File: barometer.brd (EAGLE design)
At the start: 58.4 x 40.4 mm, 91 parts, among them IC1 MIC5225-3.3v, IC2 TPS5410, IC3 ZPA2326-0311A-R, U1 MCP4725, U2 LTC2850, U3 PCA9306, U4 MAX3221, U5 XC6215XC6215B182NR, U6 Tiny85-20-SMT, X2 1751264, X3 1751248

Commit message: Migrate to customised/forked libraries
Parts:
- SJ1, SJ10, SJ11, SJ12, SJ2, SJ3, SJ4, SJ5, SJ6, SJ7, SJ8, SJ9: device SparkFun-Retired:SJ_2S-TRACE -> SparkFun-Retired-0:SJ_2S-TRACE
- U3: device SparkFun-IC-Comms:PSOP-8 -> v-shifter-sparkfun:PSOP-8
- U6: device SparkFun-Retired:SO08-EIAJ_MCU -> SparkFun-Retired-0:SO08-EIAJ_MCU
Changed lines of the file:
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@@
 <attribute name="TP_SIGNAL_NAME" value="" x="31.6625" y="17.6425" size="1" layer="38" rot="MR0"/>
 </element>
-<element name="SJ1" library="SparkFun-Retired" package="SJ_2S-TRACE" value="SOLDERJUMPERTRACE" x="55.8875" y="9.3675" smashed="yes" rot="MR90">
+<element name="SJ1" library="SparkFun-Retired-0" package="SJ_2S-TRACE" value="SOLDERJUMPERTRACE" x="55.8875" y="9.3675" smashed="yes" rot="MR90">
 <attribute name="NAME" x="53.8875" y="8.455" size="0.8128" layer="26" font="vector" ratio="18" rot="MR90"/>
 </element>
-<element name="SJ2" library="SparkFun-Retired" package="SJ_2S-TRACE" value="SOLDERJUMPERTRACE" x="52.3875" y="9.3875" smashed="yes" rot="MR90">
+<element name="SJ2" library="SparkFun-Retired-0" package="SJ_2S-TRACE" value="SOLDERJUMPERTRACE" x="52.3875" y="9.3875" smashed="yes" rot="MR90">
 <attribute name="NAME" x="51.8555" y="5.685" size="0.8128" layer="26" font="vector" ratio="18" rot="MR90"/>
 </element>
-<element name="SJ3" library="SparkFun-Retired" package="SJ_2S-TRACE" value="SOLDERJUMPERTRACE" x="47.3075" y="7.6175" smashed="yes" rot="MR90">
+<element name="SJ3" library="SparkFun-Retired-0" package="SJ_2S-TRACE" value="SOLDERJUMPERTRACE" x="47.3075" y="7.6175" smashed="yes" rot="MR90">
 <attribute name="NAME" x="45.1765" y="7.205" size="0.8128" layer="26" font="vector" ratio="18" rot="MR90"/>
 </element>
-<element name="SJ4" library="SparkFun-Retired" package="SJ_2S-TRACE" value="SOLDERJUMPERTRACE" x="49.8075" y="7.6175" smashed="yes" rot="MR90">
+<element name="SJ4" library="SparkFun-Retired-0" package="SJ_2S-TRACE" value="SOLDERJUMPERTRACE" x="49.8075" y="7.6175" smashed="yes" rot="MR90">
 <attribute name="NAME" x="47.4225" y="6.09" size="0.8128" layer="26" font="vector" ratio="18" rot="MR180"/>
 </element>
@@
 <attribute name="TP_SIGNAL_NAME" value="" x="29.1225" y="21.4525" size="1" layer="38" rot="MR0"/>
 </element>
-<element name="U6" library="SparkFun-Retired" package="SO08-EIAJ_MCU" value="Tiny85-20-SMT" x="18.0975" y="29.8425" smashed="yes" rot="MR180">
+<element name="U6" library="SparkFun-Retired-0" package="SO08-EIAJ_MCU" value="Tiny85-20-SMT" x="18.0975" y="29.8425" smashed="yes" rot="MR180">
 <attribute name="NAME" x="21.59" y="27.3025" size="0.8128" layer="26" font="vector" ratio="18" rot="MR270"/>
 <attribute name="PROD_ID" value="IC-09092" x="18.0975" y="29.8425" size="1.778" layer="28" rot="MR180" display="off"/>
 </element>
-<element name="SJ5" library="SparkFun-Retired" package="SJ_2S-TRACE" value="SOLDERJUMPERTRACE" x="24.13" y="28.89" smashed="yes">
+<element name="SJ5" library="SparkFun-Retired-0" package="SJ_2S-TRACE" value="SOLDERJUMPERTRACE" x="24.13" y="28.89" smashed="yes">
 <attribute name="NAME" x="22.36" y="26.91" size="0.8128" layer="25" font="vector" ratio="18"/>
 </element>
-<element name="SJ6" library="SparkFun-Retired" package="SJ_2S-TRACE" value="SOLDERJUMPERTRACE" x="19.05" y="30.4775" smashed="yes" rot="MR90">
+<element name="SJ6" library="SparkFun-Retired-0" package="SJ_2S-TRACE" value="SOLDERJUMPERTRACE" x="19.05" y="30.4775" smashed="yes" rot="MR90">
 <attribute name="NAME" x="20.6375" y="28.5725" size="0.8128" layer="26" font="vector" ratio="18" rot="MR90"/>
 </element>
-<element name="SJ7" library="SparkFun-Retired" package="SJ_2S-TRACE" value="SOLDERJUMPERTRACE" x="24.13" y="28.89" smashed="yes" rot="MR180">
+<element name="SJ7" library="SparkFun-Retired-0" package="SJ_2S-TRACE" value="SOLDERJUMPERTRACE" x="24.13" y="28.89" smashed="yes" rot="MR180">
 <attribute name="NAME" x="25.4" y="27.62" size="0.8128" layer="26" font="vector" ratio="18" rot="MR90"/>
 </element>
-<element name="SJ8" library="SparkFun-Retired" package="SJ_2S-TRACE" value="SOLDERJUMPERTRACE" x="24.13" y="30.795" smashed="yes" rot="MR180">
+<element name="SJ8" library="SparkFun-Retired-0" package="SJ_2S-TRACE" value="SOLDERJUMPERTRACE" x="24.13" y="30.795" smashed="yes" rot="MR180">
 <attribute name="NAME" x="25.4" y="29.8425" size="0.8128" layer="26" font="vector" ratio="18" rot="MR90"/>
 </element>
-<element name="SJ9" library="SparkFun-Retired" package="SJ_2S-TRACE" value="SOLDERJUMPERTRACE" x="17.145" y="30.4775" smashed="yes" rot="MR90">
+<element name="SJ9" library="SparkFun-Retired-0" package="SJ_2S-TRACE" value="SOLDERJUMPERTRACE" x="17.145" y="30.4775" smashed="yes" rot="MR90">
 <attribute name="NAME" x="15.28" y="31.005" size="0.8128" layer="26" font="vector" ratio="18" rot="MR0"/>
 </element>
@@
 <attribute name="OC_NEWARK" value="10R0934" x="44.02" y="3.4" size="1.778" layer="27" rot="R180" display="off"/>
 </element>
-<element name="U3" library="SparkFun-IC-Comms" package="PSOP-8" value="PCA9306" x="14.605" y="19.0475" smashed="yes" rot="R180">
+<element name="U3" library="v-shifter-sparkfun" package="PSOP-8" value="PCA9306" x="14.605" y="19.0475" smashed="yes" rot="R180">
 <attribute name="NAME" x="13.081" y="19.5475" size="0.6096" layer="21" font="vector" ratio="18" rot="SR270" align="center"/>
 <attribute name="PROD_ID" value="IC-10023" x="14.605" y="19.0475" size="1.778" layer="27" rot="R180" display="off"/>
 </element>
-<element name="SJ10" library="SparkFun-Retired" package="SJ_2S-TRACE" value="SOLDERJUMPERTRACE" x="24.75" y="35.25" smashed="yes" rot="MR180">
+<element name="SJ10" library="SparkFun-Retired-0" package="SJ_2S-TRACE" value="SOLDERJUMPERTRACE" x="24.75" y="35.25" smashed="yes" rot="MR180">
 <attribute name="NAME" x="23.7975" y="37.23" size="0.8128" layer="26" font="vector" ratio="18" rot="MR180"/>
 </element>
-<element name="SJ11" library="SparkFun-Retired" package="SJ_2S-TRACE" value="SOLDERJUMPERTRACE" x="24.75" y="35.25" smashed="yes">
+<element name="SJ11" library="SparkFun-Retired-0" package="SJ_2S-TRACE" value="SOLDERJUMPERTRACE" x="24.75" y="35.25" smashed="yes">
 <attribute name="NAME" x="23.7975" y="36.52" size="0.8128" layer="25" font="vector" ratio="18"/>
 </element>
@@
 <attribute name="TP_SIGNAL_NAME" value="" x="40.51" y="34.2675" size="1" layer="38" rot="MR0"/>
 </element>
-<element name="SJ12" library="SparkFun-Retired" package="SJ_2S-TRACE" value="SOLDERJUMPERTRACE" x="24.13" y="30.795" smashed="yes">
+<element name="SJ12" library="SparkFun-Retired-0" package="SJ_2S-TRACE" value="SOLDERJUMPERTRACE" x="24.13" y="30.795" smashed="yes">
 <attribute name="NAME" x="22.113325" y="31.9944625" size="0.8128" layer="25" font="vector" ratio="18" rot="R90" align="bottom-right"/>
 </element>

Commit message: Update all libraries
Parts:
- D2: value B340A -> 3A/40V/500mV
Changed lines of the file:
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@@
 </autorouter>
 <elements>
-<element name="D1" library="adafruit" package="SOD-123FL" value="SCHOTTKY" x="30.0075" y="13.9675" smashed="yes" rot="MR0">
+<element name="D1" library="adafruit" library_urn="urn:adsk.eagle:library:420" package="SOD-123FL" value="SCHOTTKY" x="30.0075" y="13.9675" smashed="yes" rot="MR0">
 <attribute name="NAME" x="33.6475" y="13.6975" size="0.8128" layer="26" font="vector" ratio="18" rot="MR0"/>
 </element>
-<element name="IC1" library="adafruit" package="SOT23-5L" value="MIC5225-3.3v" x="36.195" y="13.9675" smashed="yes" rot="MR90">
+<element name="IC1" library="adafruit" library_urn="urn:adsk.eagle:library:420" package="SOT23-5L" value="MIC5225-3.3v" x="36.195" y="13.9675" smashed="yes" rot="MR90">
 <attribute name="NAME" x="38.4175" y="12.6975" size="0.8128" layer="26" font="vector" ratio="18" rot="MR90"/>
 </element>
@@
 <attribute name="NAME" x="31.0515" y="23.6195" size="0.8128" layer="25" font="vector" ratio="18" rot="R270"/>
 </element>
-<element name="D2" library="SparkFun-DiscreteSemi" package="SMA-DIODE" value="B340A" x="36.5125" y="22.2225" smashed="yes">
+<element name="D2" library="SparkFun-DiscreteSemi" library_urn="urn:adsk.eagle:library:514" package="SMA-DIODE" package3d_urn="urn:adsk.eagle:package:38443/1" value="3A/40V/500mV" x="36.5125" y="22.2225" smashed="yes">
 <attribute name="NAME" x="37.465" y="23.8735" size="0.8128" layer="25" font="vector" ratio="18"/>
 <attribute name="PROD_ID" value="DIO-09886" x="36.5125" y="22.2225" size="1.778" layer="27" display="off"/>

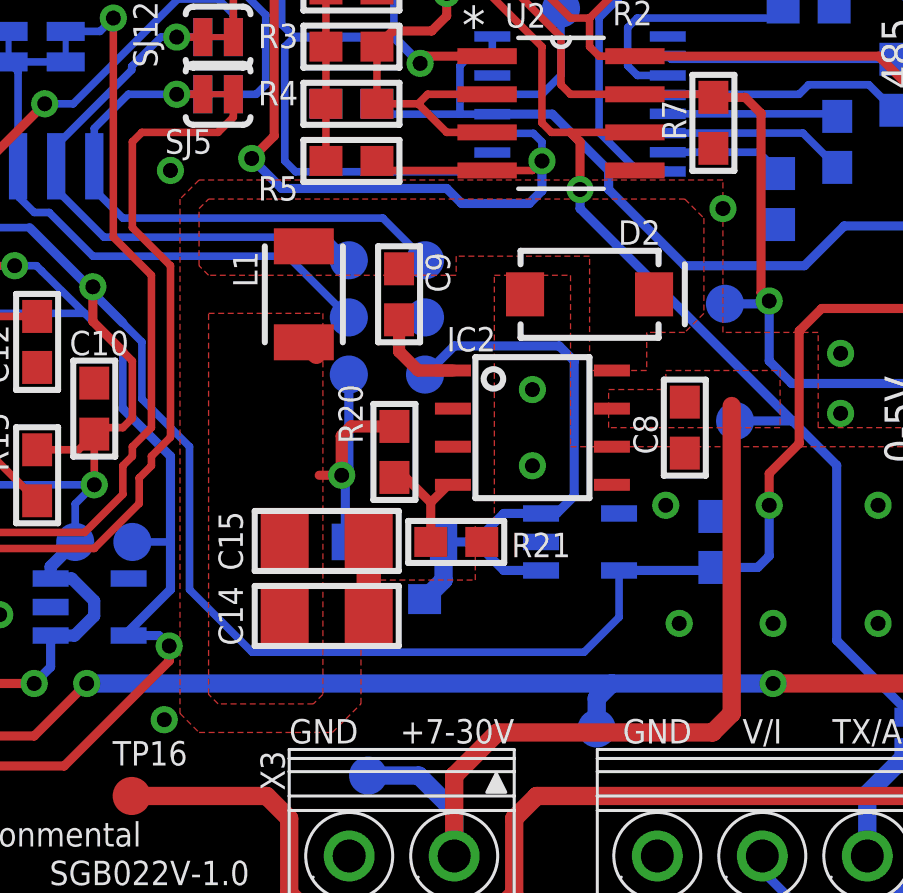
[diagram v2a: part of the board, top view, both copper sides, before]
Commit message: Fix inductor's footprint's dimensions
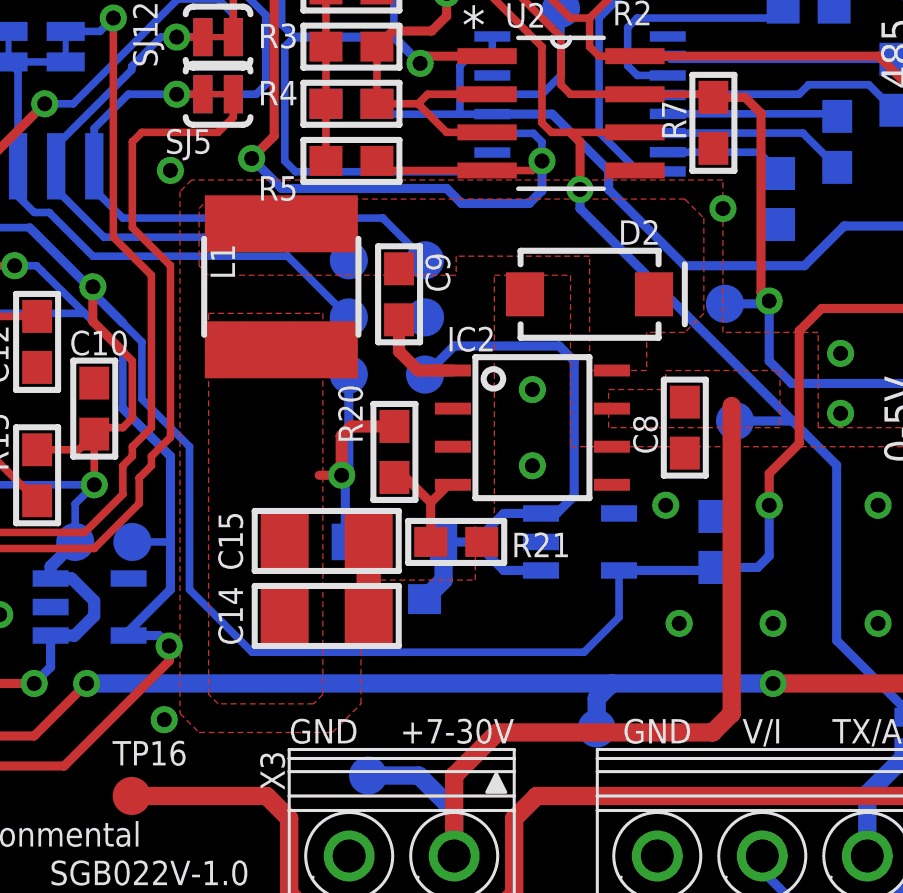
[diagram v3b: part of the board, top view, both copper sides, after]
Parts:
- L1: device Particle:1210 -> inductor-tdk:VLS6045EX
- moved L1 0.79 mm to (26.2, 22.5)
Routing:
- net +5V0: track 10.3 -> 10.9 mm
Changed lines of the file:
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@@
 <attribute name="PROD_ID" value="DIO-09886" x="36.5125" y="22.2225" size="1.778" layer="27" display="off"/>
 </element>
-<element name="L1" library="Particle" package="1210" value="68u" x="26.9875" y="22.2225" smashed="yes" rot="R270">
-<attribute name="NAME" x="24.63" y="23.6575" size="0.8128" layer="25" font="vector" ratio="18" rot="R270"/>
+<element name="L1" library="inductor-tdk" package="VLS6045EX" value="68u" x="26.2375" y="22.4725" smashed="yes" rot="R270">
+<attribute name="NAME" x="23.88" y="23.9075" size="0.8128" layer="25" font="vector" ratio="18" rot="R270"/>
 </element>
 <element name="R20" library="microbuilder" package="0603" value="10k" x="30.0075" y="16.9675" smashed="yes" rot="R90">
@@
 <vertex x="40.9575" y="20.9525"/>
 <vertex x="40.9575" y="26.0325"/>
-<vertex x="23.495" y="26.0325"/>
-<vertex x="22.86" y="25.3975"/>
+<vertex x="23.245" y="26.0325"/>
+<vertex x="22.86" y="25.6475"/>
 <vertex x="22.86" y="8.2525"/>
 <vertex x="23.495" y="7.6175"/>
@@
 <contactref element="C14" pad="1"/>
 <contactref element="R20" pad="2"/>
-<wire x1="27.4075" y1="20.2025" x2="26.9875" y2="20.6225" width="0.6096" layer="1"/>
+<wire x1="27.4075" y1="20.2025" x2="26.2375" y2="20.3725" width="0.6096" layer="1"/>
 <contactref element="TP1" pad="TP"/>
 <polygon width="0.3048" layer="1">

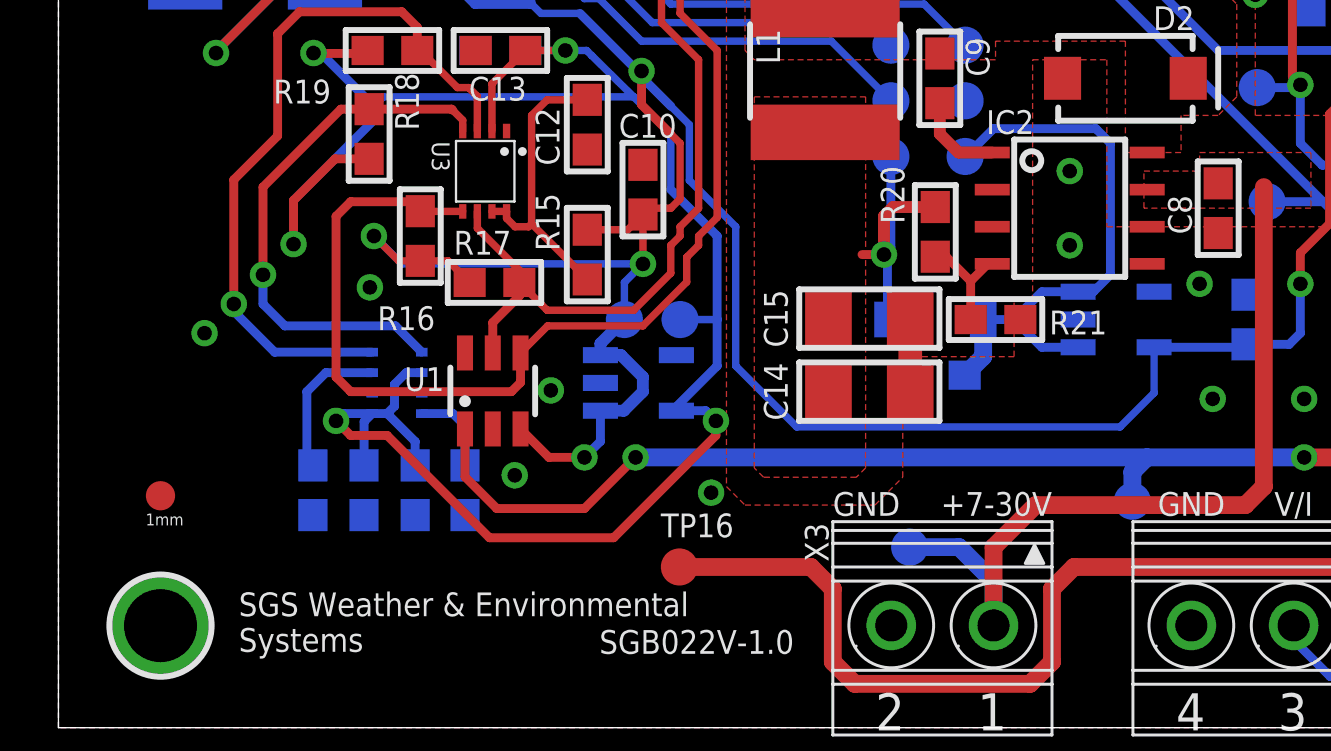
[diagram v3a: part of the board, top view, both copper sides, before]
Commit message: Fix DAC output's voltage reference from +3V3 to +5V0
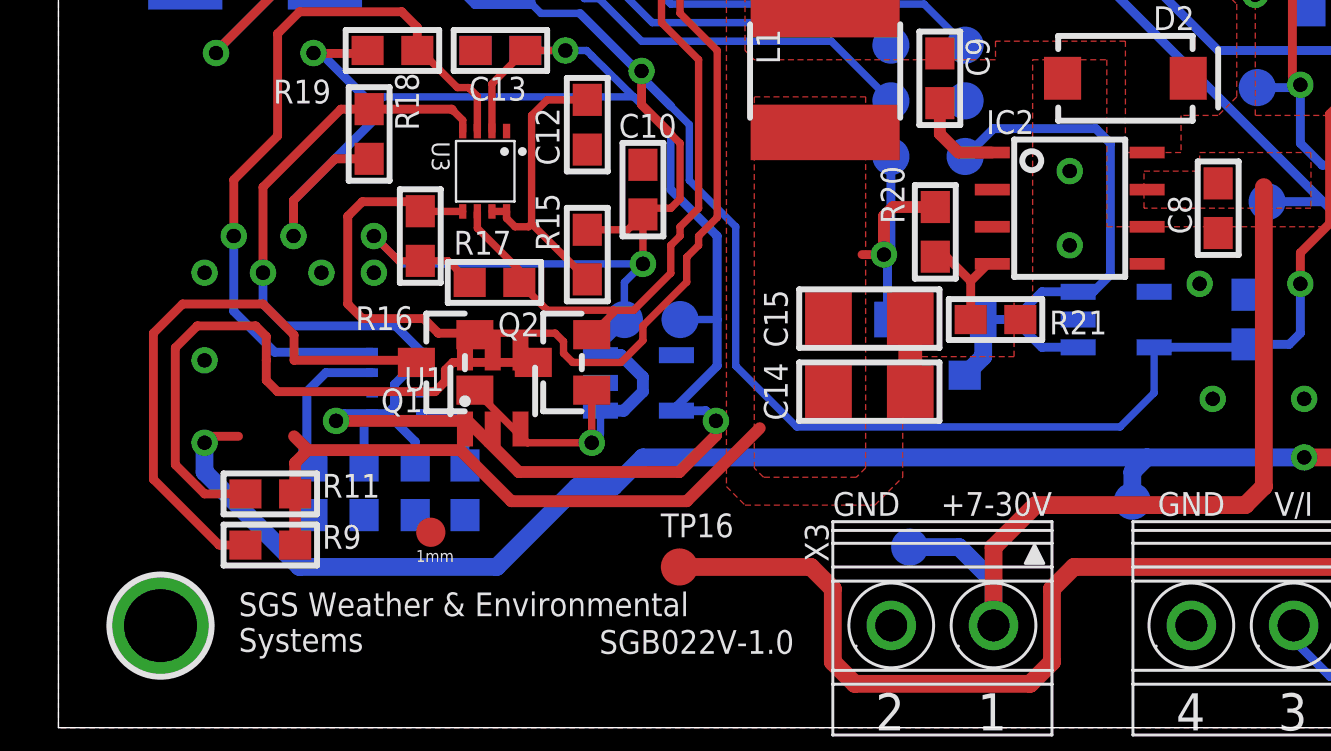
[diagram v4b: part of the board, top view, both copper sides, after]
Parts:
- added Q1, Q2: (no value), microbuilder:SOT23-WIDE
- added R11, R9: 10k, microbuilder:0603
- moved FID2 9.33 mm to (12.7, 6.69)
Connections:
- new net SCL_5V0: Q2.3, R11.1, U1.5
- new net SDA_5V0: Q1.3, R9.1, U1.4
- net +3V3: now also Q1.1, Q2.1; no longer U1.3
- net +5V0: now also R11.2, R9.2, U1.3
- net SCL_3V3: now also Q2.2; no longer U1.5
- net SDA_3V3: now also Q1.2; no longer U1.4
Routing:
- net SCL_5V0: track 0.00 -> 21.8 mm
- net +5V0: track 10.9 -> 32.2 mm
- net SDA_5V0: track 0.00 -> 19.8 mm
- net V-OUT: track 43.6 -> 54.9 mm
- net +3V3: track 112.8 -> 116.1 mm
- net SDA_3V3: track 42.0 -> 38.9 mm
- net +1V8: track 73.2 -> 70.8 mm
- net SCL_3V3: track 30.5 -> 28.8 mm
- net GND: vias 26 -> 25

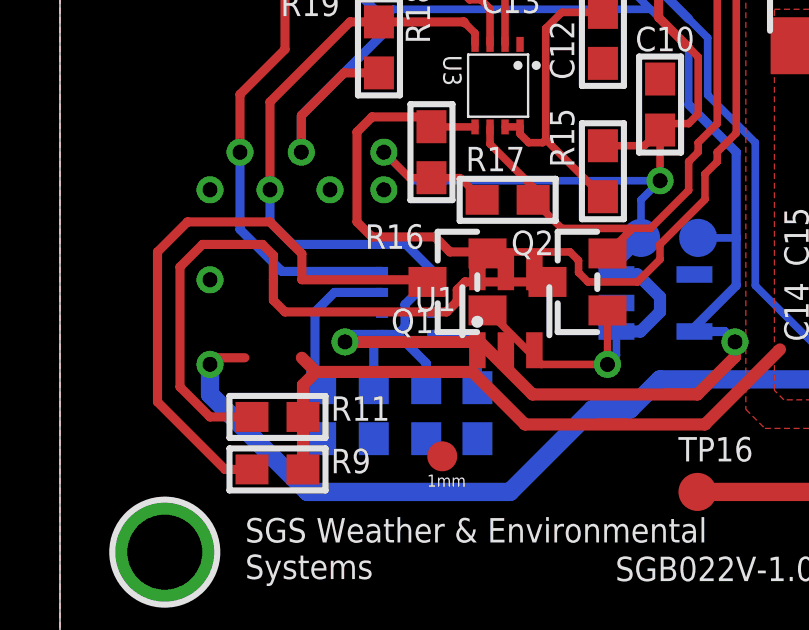
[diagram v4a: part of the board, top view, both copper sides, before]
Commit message: Indicate the I2C slave address corresponding to the evaluated DAC
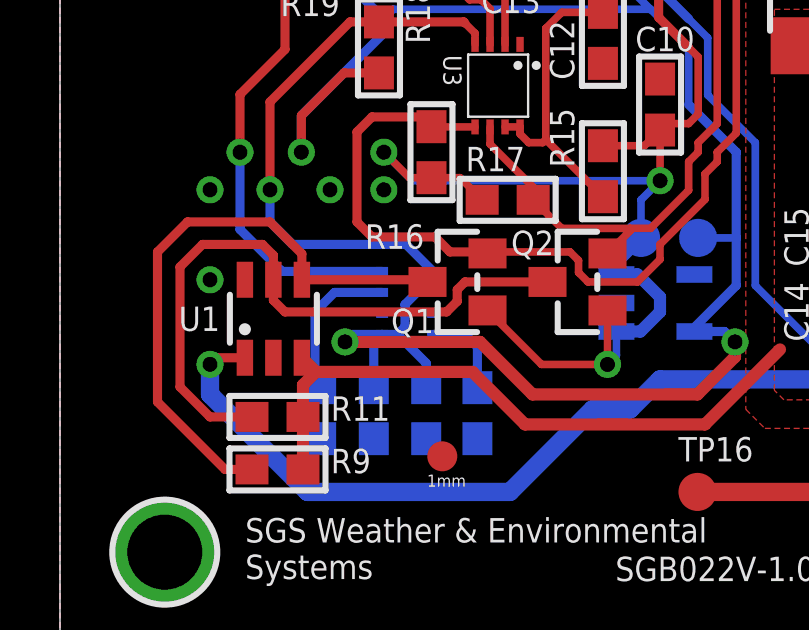
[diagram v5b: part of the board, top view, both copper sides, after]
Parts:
- U1: value MCP4725 -> MCP4725A0
- moved U1 7.75 mm to (7.11, 11.3)
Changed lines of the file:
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@@
 <attribute name="NAME" x="15.28" y="31.005" size="0.8128" layer="26" font="vector" ratio="18" rot="MR0"/>
 </element>
-<element name="U1" library="microbuilder" package="SOT23-6" value="MCP4725" x="14.8625" y="11.5225" smashed="yes">
-<attribute name="NAME" x="11.831" y="11.5225" size="0.8128" layer="25" font="vector" ratio="18"/>
+<element name="U1" library="microbuilder" package="SOT23-6" value="MCP4725A0" x="7.1125" y="11.2725" smashed="yes">
+<attribute name="NAME" x="5.331" y="11.2725" size="0.8128" layer="25" font="vector" ratio="18" align="center-right"/>
 </element>
 <element name="X3" library="con-phoenix-350" library_urn="urn:adsk.eagle:library:174" package="1751248" package3d_urn="urn:adsk.eagle:package:9395/1" value="1751248" x="30.25" y="3.4" smashed="yes" rot="R180">
